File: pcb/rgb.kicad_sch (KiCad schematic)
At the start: 27 parts, among them J1 Conn_02x08_Odd_Even, J3 B4PS-VH, J4 TYPE-C-31-M-12, J5 TF-01A, J7 B4PS-VH, U4 WIFI, U5 ESP32-WROOM-32E, U7 CH340C, U8 SPX3819M5-L, U9 CH224K

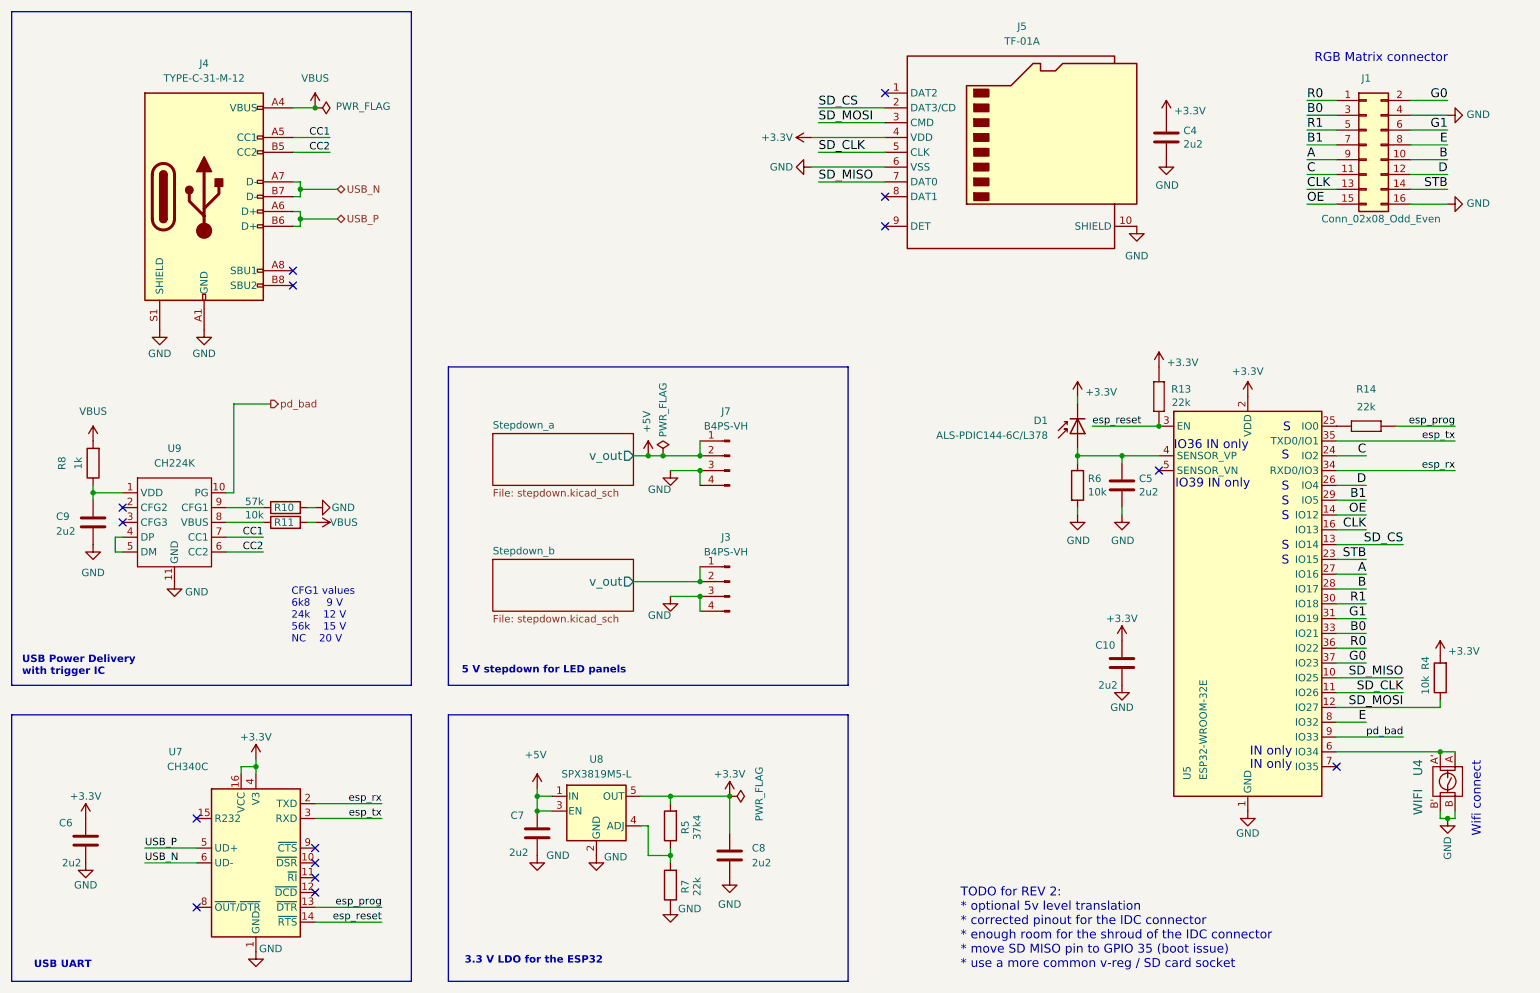
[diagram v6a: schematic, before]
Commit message: mostly ready for production. 18 $ / board in qty. 5
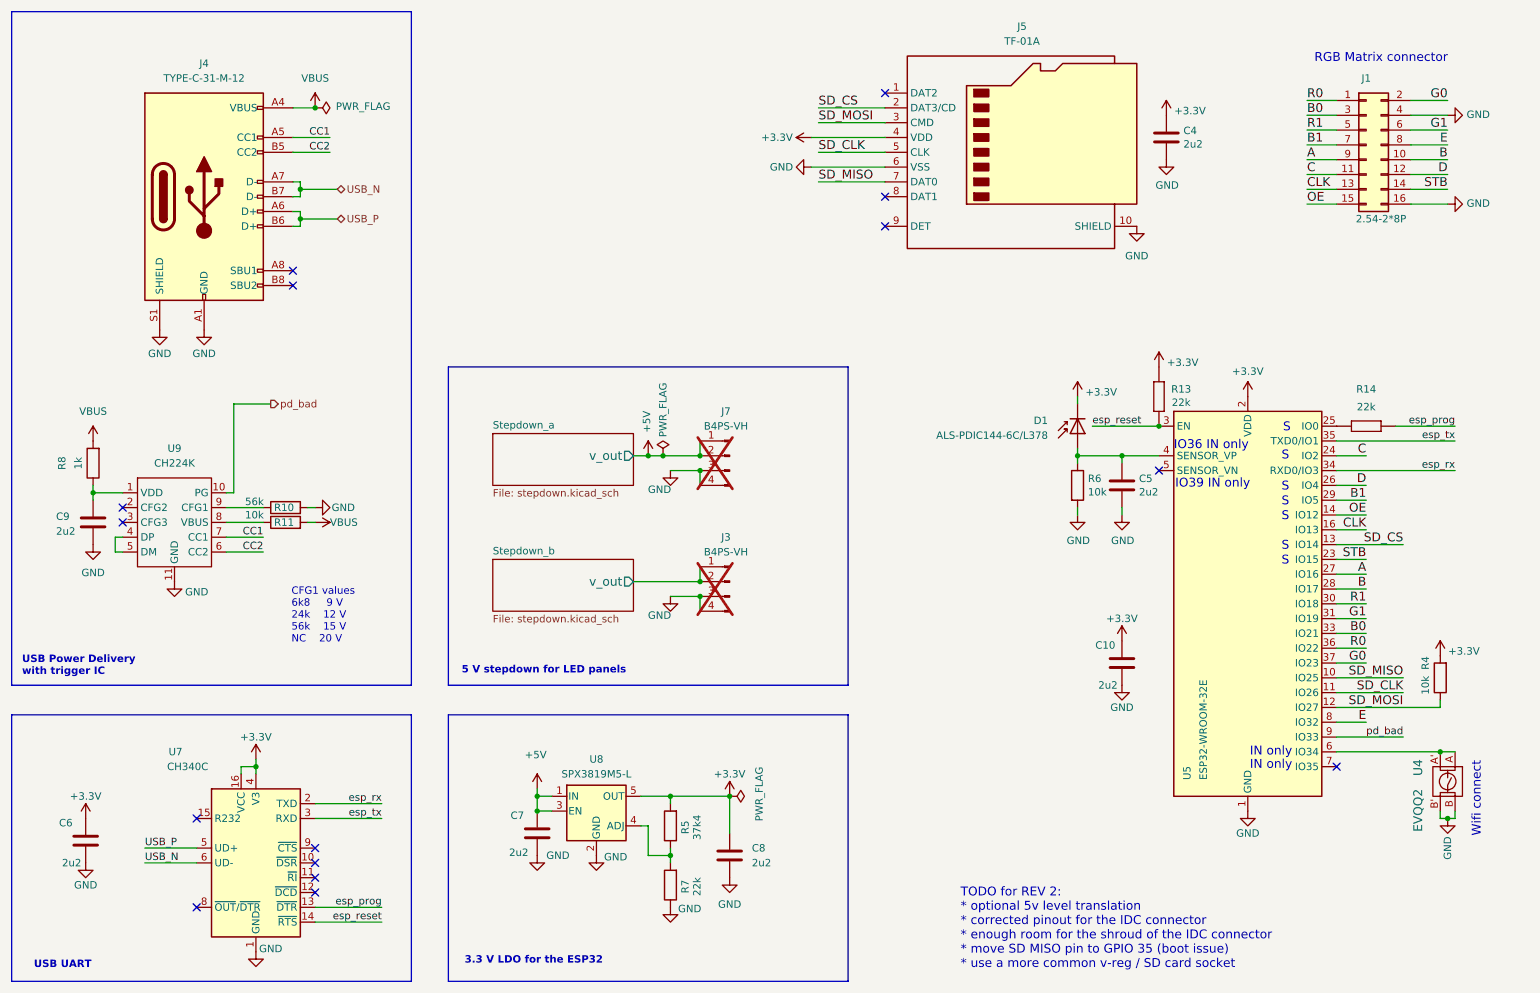
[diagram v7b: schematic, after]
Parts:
- J1: value Conn_02x08_Odd_Even -> 2.54-2*8P
- J3, J7: now not fitted; now left out of the parts list
- R10: value 57k -> 56k
- U4: value WIFI -> EVQQ2
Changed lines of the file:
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@@
 			)
 		)
-		(property "Value" "Conn_02x08_Odd_Even"
+		(property "Value" "2.54-2*8P"
 			(at 255.27 52.07 0)
 			(effects
@@
 			)
 		)
-		(property "Value" "WIFI"
+		(property "Value" "EVQQ2"
 			(at 261.62 149.86 0)
 			(effects
@@
 		(unit 1)
 		(exclude_from_sim no)
-		(in_bom yes)
+		(in_bom no)
 		(on_board yes)
-		(dnp no)
+		(dnp yes)
 		(property "Reference" "J7"
 			(at 142.875 85.09 0)
@@
 		(unit 1)
 		(exclude_from_sim no)
-		(in_bom yes)
+		(in_bom no)
 		(on_board yes)
-		(dnp no)
+		(dnp yes)
 		(property "Reference" "J3"
 			(at 142.875 106.68 0)
@@
 			)
 		)
-		(property "Value" "57k"
+		(property "Value" "56k"
 			(at 61.976 100.584 90)
 			(effects

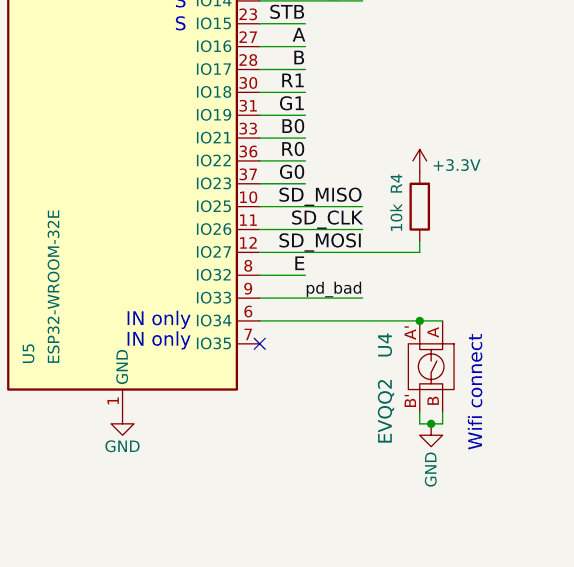
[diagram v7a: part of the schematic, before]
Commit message: add pattern to top silkscreen, order
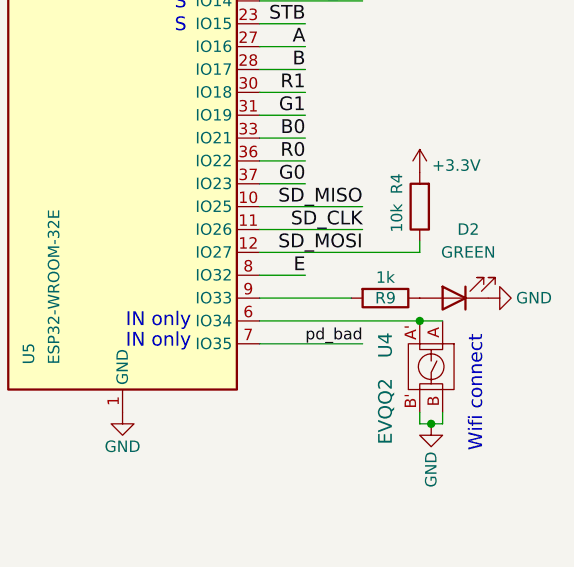
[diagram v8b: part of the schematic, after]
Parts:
- added D2: GREEN, LED_SMD:LED_0603_1608Metric, symbol Device:LED
- added R9: 1k, Resistor_SMD:R_0603_1608Metric, symbol Device:R
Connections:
- net GND: now also D2.1 (K)
- net pd_bad: now also U5.7 (IO35); no longer U5.9 (IO33)
- new net: D2.2 (A), R9.1
- new net: R9.2, U5.9 (IO33)
- no-connect marks 15 -> 14
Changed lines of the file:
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@@
 	)
 	(no_connect
-		(at 247.65 146.05)
-	)
-	(no_connect
 		(at 217.17 95.25)
 	)
@@
 	(wire
 		(pts
+			(xy 247.65 140.97) (xy 257.81 140.97)
+		)
+		(stroke
+			(width 0)
+			(type default)
+		)
+	)
+	(wire
+		(pts
 			(xy 265.43 134.62) (xy 265.43 135.89)
 		)
@@
 	(wire
 		(pts
-			(xy 247.65 140.97) (xy 259.08 140.97)
+			(xy 247.65 146.05) (xy 259.08 146.05)
 		)
 		(stroke
@@
 	)
 	(label "pd_bad"
-		(at 259.08 140.97 180)
+		(at 259.08 146.05 180)
 		(fields_autoplaced yes)
 		(effects
@@
 	)
 	(symbol
+		(lib_id "Device:LED")
+		(at 269.24 140.97 180)
+		(unit 1)
+		(exclude_from_sim no)
+		(in_bom yes)
+		(on_board yes)
+		(dnp no)
+		(fields_autoplaced yes)
+		(property "Reference" "D2"
+			(at 270.8275 133.35 0)
+			(effects
+				(font
+					(size 1.27 1.27)
+				)
+			)
+		)
+		(property "Value" "GREEN"
+			(at 270.8275 135.89 0)
+			(effects
+				(font
+					(size 1.27 1.27)
+				)
+			)
+		)
+		(property "Footprint" "LED_SMD:LED_0603_1608Metric"
+			(at 269.24 140.97 0)
+			(effects
+				(font
+					(size 1.27 1.27)
+				)
+				(hide yes)
+			)
+		)
+		(property "Datasheet" "~"
+			(at 269.24 140.97 0)
+			(effects
+				(font
+					(size 1.27 1.27)
+				)
+				(hide yes)
+			)
+		)
+		(property "Description" "Light emitting diode"
+			(at 269.24 140.97 0)
+			(effects
+				(font
+					(size 1.27 1.27)
+				)
+				(hide yes)
+			)
+		)
+		(pin "2"
+		)
+		(pin "1"
+		)
+		(instances
+			(project "rgb"
+				(path "/e2cadc20-e108-4c6f-b279-00d9d28fa9da"
+					(reference "D2")
+					(unit 1)
+				)
+			)
+		)
+	)
+	(symbol
 		(lib_id "Device:R")
 		(at 133.35 156.21 180)
@@
 	)
 	(symbol
+		(lib_id "Device:R")
+		(at 261.62 140.97 270)
+		(unit 1)
+		(exclude_from_sim no)
+		(in_bom yes)
+		(on_board yes)
+		(dnp no)
+		(property "Reference" "R9"
+			(at 261.62 140.97 90)
+			(effects
+				(font
+					(size 1.27 1.27)
+				)
+			)
+		)
+		(property "Value" "1k"
+			(at 261.62 138.684 90)
+			(effects
+				(font
+					(size 1.27 1.27)
+				)
+			)
+		)
+		(property "Footprint" "Resistor_SMD:R_0603_1608Metric"
+			(at 261.62 139.192 90)
+			(effects
+				(font
+					(size 1.27 1.27)
+				)
+				(hide yes)
+			)
+		)
+		(property "Datasheet" "~"
+			(at 261.62 140.97 0)
+			(effects
+				(font
+					(size 1.27 1.27)
+				)
+				(hide yes)
+			)
+		)
+		(property "Description" "Resistor"
+			(at 261.62 140.97 0)
+			(effects
+				(font
+					(size 1.27 1.27)
+				)
+				(hide yes)
+			)
+		)
+		(pin "2"
+		)
+		(pin "1"
+		)
+		(instances
+			(project "rgb"
+				(path "/e2cadc20-e108-4c6f-b279-00d9d28fa9da"
+					(reference "R9")
+					(unit 1)
+				)
+			)
+		)
+	)
+	(symbol
 		(lib_id "power:GND")
 		(at 48.26 114.3 0)
@@
 					(unit 1)
 				)
+			)
+		)
+	)
+	(symbol
+		(lib_id "power:GND")
+		(at 273.05 140.97 90)
+		(unit 1)
+		(exclude_from_sim no)
+		(in_bom yes)
+		(on_board yes)
+		(dnp no)
+		(property "Reference" "#PWR016"
+			(at 279.4 140.97 0)
+			(effects
+				(font
+					(size 1.27 1.27)
+				)
+				(hide yes)
+			)
+		)
+		(property "Value" "GND"
+			(at 278.13 140.97 90)
+			(effects
+				(font
+					(size 1.27 1.27)
+				)
+			)
+		)
+		(property "Footprint" ""
+			(at 273.05 140.97 0)
+			(effects
+				(font
+					(size 1.27 1.27)
+				)
+				(hide yes)
+			)
+		)
+		(property "Datasheet" ""
+			(at 273.05 140.97 0)
+			(effects
+				(font
+					(size 1.27 1.27)
+				)
+				(hide yes)
+			)
+		)
+		(property "Description" ""
+			(at 273.05 140.97 0)
+			(effects
+				(font
+					(size 1.27 1.27)
+				)
+				(hide yes)
+			)
+		)
+		(pin "1"
+		)
+		(instances
+			(project "rgb"
+				(path "/e2cadc20-e108-4c6f-b279-00d9d28fa9da"
+					(reference "#PWR016")
+					(unit 1)
+				)
